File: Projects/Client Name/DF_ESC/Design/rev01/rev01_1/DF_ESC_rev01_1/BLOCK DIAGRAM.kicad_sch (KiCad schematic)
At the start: 0 parts

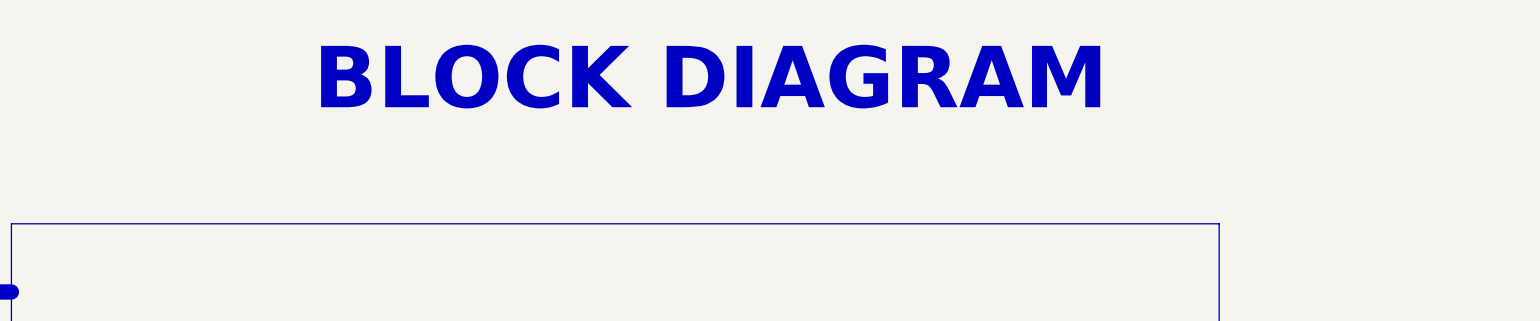
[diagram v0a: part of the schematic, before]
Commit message: Update 19-01-2024 primera
cambiar y añadir numeracion de sheets
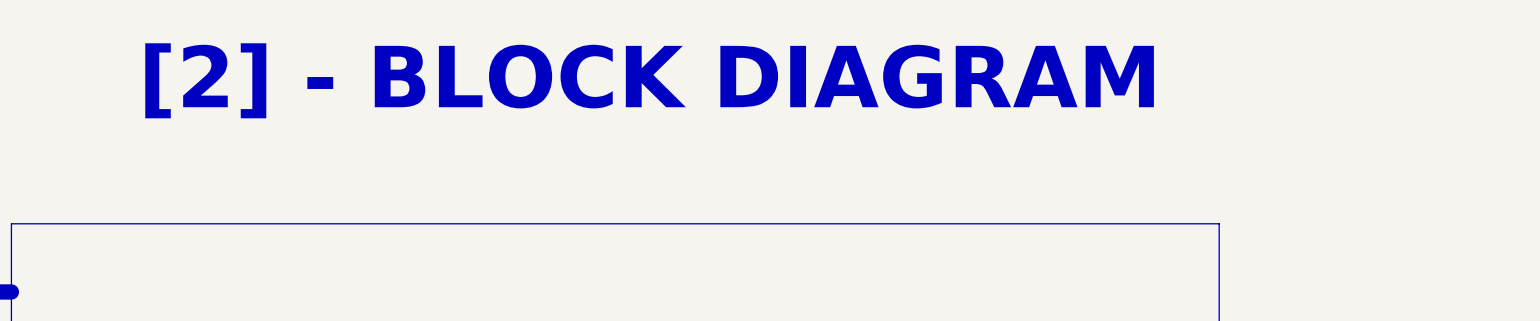
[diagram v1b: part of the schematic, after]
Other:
- note added: "[2] - BLOCK DIAGRAM"
- note removed: "BLOCK DIAGRAM"
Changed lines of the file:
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@@
     (effects (font (size 3 3) bold) (justify left bottom))
   )
-  (text "BLOCK DIAGRAM" (at 110.49 27.94 0)
+  (text "[2] - BLOCK DIAGRAM" (at 87.63 27.94 0)
     (effects (font (size 8 8) bold) (justify left bottom))
   )

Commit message: Update 2024-02-28_2
Input Proteccion Done
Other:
- note added: "Page 1"
- note added: "Page 3"
- note added: "Page 4"
- note added: "Page 5"
- note added: "Page 6"
- note added: "Page 7"
- note added: "Page 8"
- note added: "Page 9"
- note added: "STEP-DOWN 3V3"
- note added: "[1] - BLOCK DIAGRAM"
- note removed: "[2] - BLOCK DIAGRAM"
